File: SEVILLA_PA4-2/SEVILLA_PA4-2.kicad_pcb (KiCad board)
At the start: 2 copper layers, 100 x 50 mm, 15 parts, among them J1 Conn_01x02, SW3 SW_SPST, SW4 SW_SPST, U1 HDSP-7401, U2 PIC16F84A-XXP, U3 HDSP-7401, Y1 4 MHz

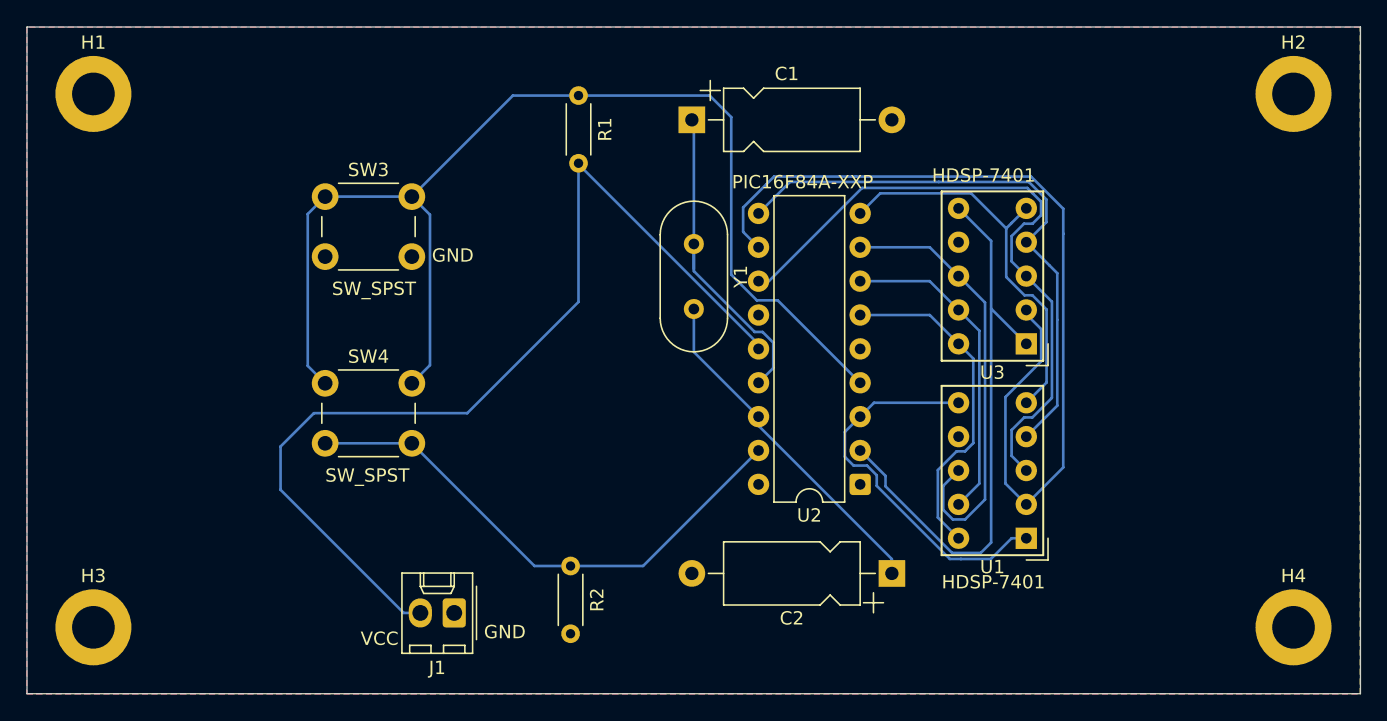
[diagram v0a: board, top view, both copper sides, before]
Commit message: Refactor code structure and remove redundant code blocks for improved readability and maintainability
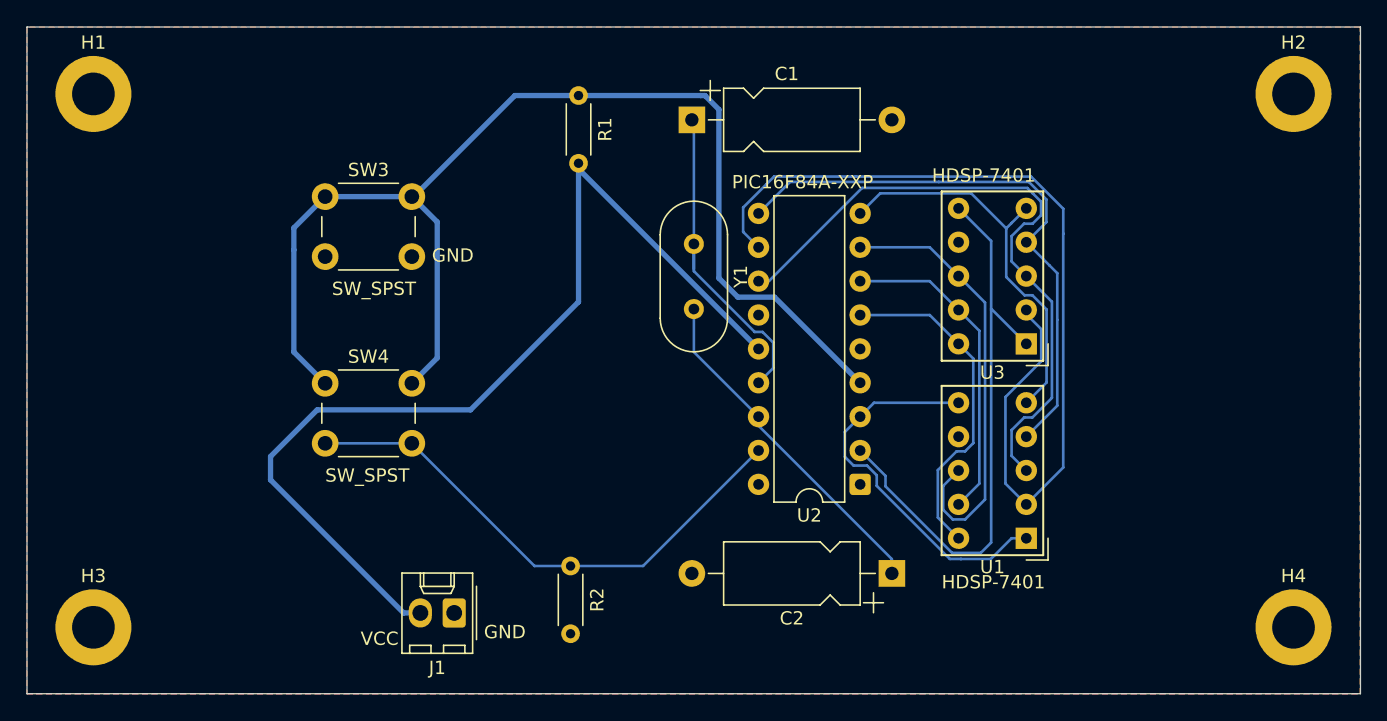
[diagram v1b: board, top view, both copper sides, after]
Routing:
- net Net-(SW3-A): track 89.3 -> 91.1 mm
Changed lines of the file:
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@@
 	)
 	(segment
-		(start 126.985 105.48)
-		(end 117.75 96.245)
-		(width 0.2)
+		(start 140.0966 72.17945)
+		(end 140.0966 71.75945)
+		(width 0.4)
+		(layer "B.Cu")
+		(net 4)
+	)
+	(segment
+		(start 132 90.25)
+		(end 140.0966 82.1534)
+		(width 0.4)
+		(layer "B.Cu")
+		(net 4)
+	)
+	(segment
+		(start 128.235 105.48)
+		(end 126.98 105.48)
+		(width 0.4)
+		(layer "B.Cu")
+		(net 4)
+	)
+	(segment
+		(start 117 93.75)
+		(end 120.5 90.25)
+		(width 0.4)
+		(layer "B.Cu")
+		(net 4)
+	)
+	(segment
+		(start 153.5966 85.67945)
+		(end 140.0966 72.17945)
+		(width 0.4)
 		(layer "B.Cu")
 		(net 4)
@@
 		(start 140.0966 82.1534)
 		(end 140.0966 71.75945)
-		(width 0.2)
+		(width 0.4)
 		(layer "B.Cu")
 		(net 4)
 	)
 	(segment
-		(start 120.25 90.5)
-		(end 131.75 90.5)
-		(width 0.2)
+		(start 126.98 105.48)
+		(end 117 95.5)
+		(width 0.4)
 		(layer "B.Cu")
 		(net 4)
 	)
 	(segment
-		(start 140.0966 71.83185)
-		(end 153.5966 85.33185)
-		(width 0.2)
+		(start 117 95.5)
+		(end 117 93.75)
+		(width 0.4)
 		(layer "B.Cu")
 		(net 4)
 	)
 	(segment
-		(start 140.0966 71.75945)
-		(end 140.0966 71.83185)
-		(width 0.2)
-		(layer "B.Cu")
-		(net 4)
-	)
-	(segment
-		(start 128.235 106.23)
-		(end 127.735 106.23)
-		(width 0.2)
-		(layer "B.Cu")
-		(net 4)
-	)
-	(segment
-		(start 117.75 96.245)
-		(end 117.75 93)
-		(width 0.2)
-		(layer "B.Cu")
-		(net 4)
-	)
-	(segment
-		(start 153.5966 85.33185)
-		(end 153.5966 85.67945)
-		(width 0.2)
-		(layer "B.Cu")
-		(net 4)
-	)
-	(segment
-		(start 117.75 93)
-		(end 120.25 90.5)
-		(width 0.2)
-		(layer "B.Cu")
-		(net 4)
-	)
-	(segment
-		(start 128.235 105.48)
-		(end 126.985 105.48)
-		(width 0.2)
-		(layer "B.Cu")
-		(net 4)
-	)
-	(segment
-		(start 131.75 90.5)
-		(end 140.0966 82.1534)
-		(width 0.2)
+		(start 120.5 90.25)
+		(end 132 90.25)
+		(width 0.4)
 		(layer "B.Cu")
 		(net 4)
@@
 	)
 	(segment
-		(start 155.0349 82.03775)
-		(end 153.4723 82.03775)
-		(width 0.2)
+		(start 127.5966 74.25945)
+		(end 127.74055 74.25945)
+		(width 0.4)
+		(layer "B.Cu")
+		(net 19)
+	)
+	(segment
+		(start 149.25 66.67945)
+		(end 140.0966 66.67945)
+		(width 0.4)
+		(layer "B.Cu")
+		(net 19)
+	)
+	(segment
+		(start 129.5 86.35605)
+		(end 129.5 76.16285)
+		(width 0.4)
+		(layer "B.Cu")
+		(net 19)
+	)
+	(segment
+		(start 127.74055 74.25945)
+		(end 135.32055 66.67945)
+		(width 0.4)
+		(layer "B.Cu")
+		(net 19)
+	)
+	(segment
+		(start 127.5966 88.25945)
+		(end 129.5 86.35605)
+		(width 0.4)
+		(layer "B.Cu")
+		(net 19)
+	)
+	(segment
+		(start 121.0966 88.25945)
+		(end 118.75 85.91285)
+		(width 0.4)
+		(layer "B.Cu")
+		(net 19)
+	)
+	(segment
+		(start 129.5 76.16285)
+		(end 127.5966 74.25945)
+		(width 0.4)
+		(layer "B.Cu")
+		(net 19)
+	)
+	(segment
+		(start 154.7976 81.80045)
+		(end 152.05045 81.80045)
+		(width 0.4)
+		(layer "B.Cu")
+		(net 19)
+	)
+	(segment
+		(start 150.625 67.72835)
+		(end 149.5761 66.67945)
+		(width 0.4)
+		(layer "B.Cu")
+		(net 19)
+	)
+	(segment
+		(start 118.75 78.25)
+		(end 118.75 76.60605)
+		(width 0.4)
+		(layer "B.Cu")
+		(net 19)
+	)
+	(segment
+		(start 150.625 80.375)
+		(end 150.625 67.72835)
+		(width 0.4)
+		(layer "B.Cu")
+		(net 19)
+	)
+	(segment
+		(start 118.75 76.60605)
+		(end 121.0966 74.25945)
+		(width 0.4)
+		(layer "B.Cu")
+		(net 19)
+	)
+	(segment
+		(start 152.05045 81.80045)
+		(end 150.625 80.375)
+		(width 0.4)
 		(layer "B.Cu")
 		(net 19)
@@
 		(start 121.0966 74.25945)
 		(end 127.5966 74.25945)
-		(width 0.2)
-		(layer "B.Cu")
-		(net 19)
-	)
-	(segment
-		(start 135.1766 66.67945)
-		(end 127.5966 74.25945)
-		(width 0.2)
-		(layer "B.Cu")
-		(net 19)
-	)
-	(segment
-		(start 128.9578 75.62065)
-		(end 127.5966 74.25945)
-		(width 0.2)
-		(layer "B.Cu")
-		(net 19)
-	)
-	(segment
-		(start 151.5504 80.11585)
-		(end 151.5504 68.3004)
-		(width 0.2)
-		(layer "B.Cu")
-		(net 19)
-	)
-	(segment
-		(start 128.9578 86.89825)
-		(end 128.9578 75.62065)
-		(width 0.2)
-		(layer "B.Cu")
-		(net 19)
-	)
-	(segment
-		(start 153.4723 82.03775)
-		(end 151.5504 80.11585)
-		(width 0.2)
-		(layer "B.Cu")
-		(net 19)
-	)
-	(segment
-		(start 119.7897 86.95255)
-		(end 119.7897 75.56635)
-		(width 0.2)
-		(layer "B.Cu")
-		(net 19)
-	)
-	(segment
-		(start 149.92945 66.67945)
+		(width 0.4)
+		(layer "B.Cu")
+		(net 19)
+	)
+	(segment
+		(start 118.75 85.91285)
+		(end 118.75 78.25)
+		(width 0.4)
+		(layer "B.Cu")
+		(net 19)
+	)
+	(segment
+		(start 149.5761 66.67945)
+		(end 149.25 66.67945)
+		(width 0.4)
+		(layer "B.Cu")
+		(net 19)
+	)
+	(segment
+		(start 135.32055 66.67945)
 		(end 140.0966 66.67945)
-		(width 0.2)
-		(layer "B.Cu")
-		(net 19)
-	)
-	(segment
-		(start 119.7897 75.56635)
-		(end 121.0966 74.25945)
-		(width 0.2)
+		(width 0.4)
 		(layer "B.Cu")
 		(net 19)
@@
 	(segment
 		(start 161.2166 88.21945)
-		(end 155.0349 82.03775)
-		(width 0.2)
-		(layer "B.Cu")
-		(net 19)
-	)
-	(segment
-		(start 121.0966 88.25945)
-		(end 119.7897 86.95255)
-		(width 0.2)
-		(layer "B.Cu")
-		(net 19)
-	)
-	(segment
-		(start 140.0966 66.67945)
-		(end 135.1766 66.67945)
-		(width 0.2)
-		(layer "B.Cu")
-		(net 19)
-	)
-	(segment
-		(start 151.5504 68.3004)
-		(end 149.92945 66.67945)
-		(width 0.2)
-		(layer "B.Cu")
-		(net 19)
-	)
-	(segment
-		(start 127.5966 88.25945)
-		(end 128.9578 86.89825)
-		(width 0.2)
-		(layer "B.Cu")
-		(net 19)
+		(end 154.7976 81.80045)
+		(width 0.4)
+		(layer "B.Cu")
+		(net 19)

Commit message: Add lock files for PCB and schematic with user session details
- Created lock file for SEVILLA_PA4-2.kicad_pcb with hostname and username.
- Created lock file for SEVILLA_PA4-2.kicad_sch with hostname and username.
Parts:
- moved H1 0.07 mm to (103.8, 66.5)
- moved H2 0.07 mm to (193.8, 66.5)
- moved H3 0.07 mm to (103.8, 106.5)
- moved H4 0.07 mm to (193.8, 106.5)
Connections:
- H1 pad 1: unconnected-(H1-Pad1) -> GND
- H2 pad 1: unconnected-(H2-Pad1) -> GND
- H3 pad 1: unconnected-(H3-Pad1) -> GND
- H4 pad 1: unconnected-(H4-Pad1) -> GND
